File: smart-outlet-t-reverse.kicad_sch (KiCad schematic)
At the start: 4 parts

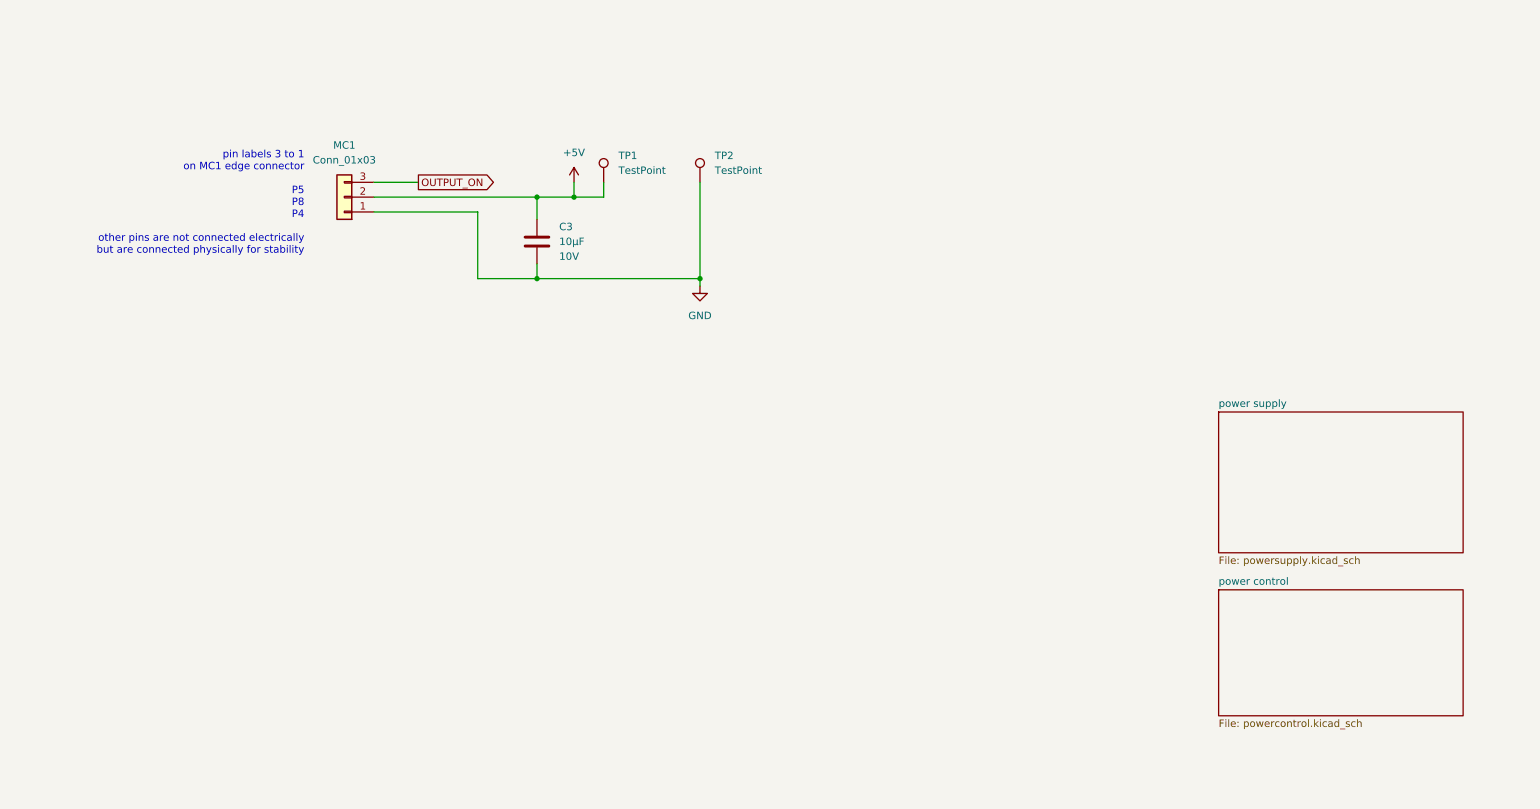
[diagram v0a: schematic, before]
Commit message: Cleaned schematic. Still have silk and fab to do. Also have not fixed F1. Have decided I may not fix F1.
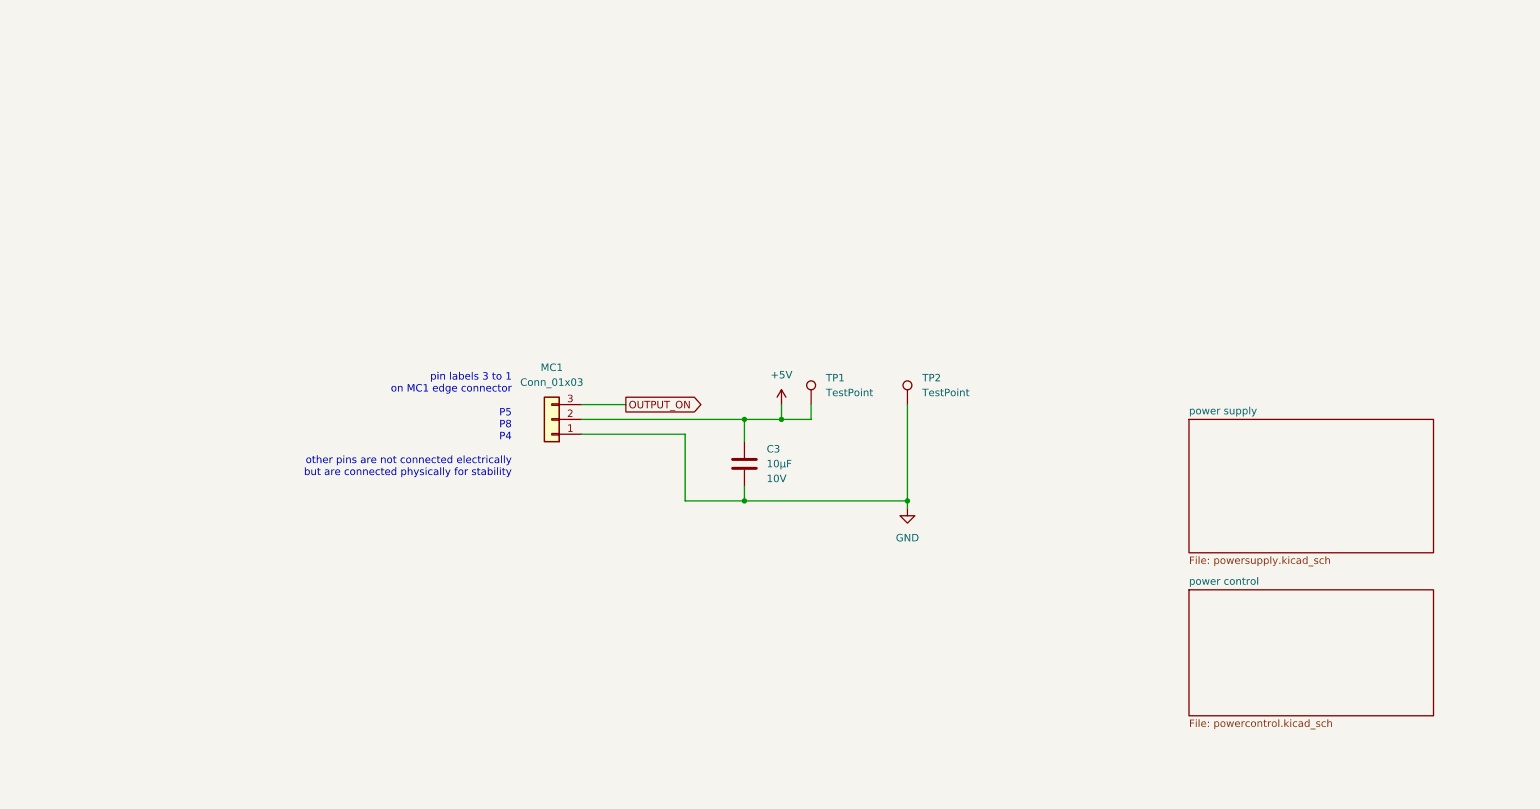
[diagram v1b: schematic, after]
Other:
- title: (none) -> T smart switched power outlet
- moved on the sheet: C3, MC1, TP1, TP2

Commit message: Added description of microcontroller subboard to schematic.
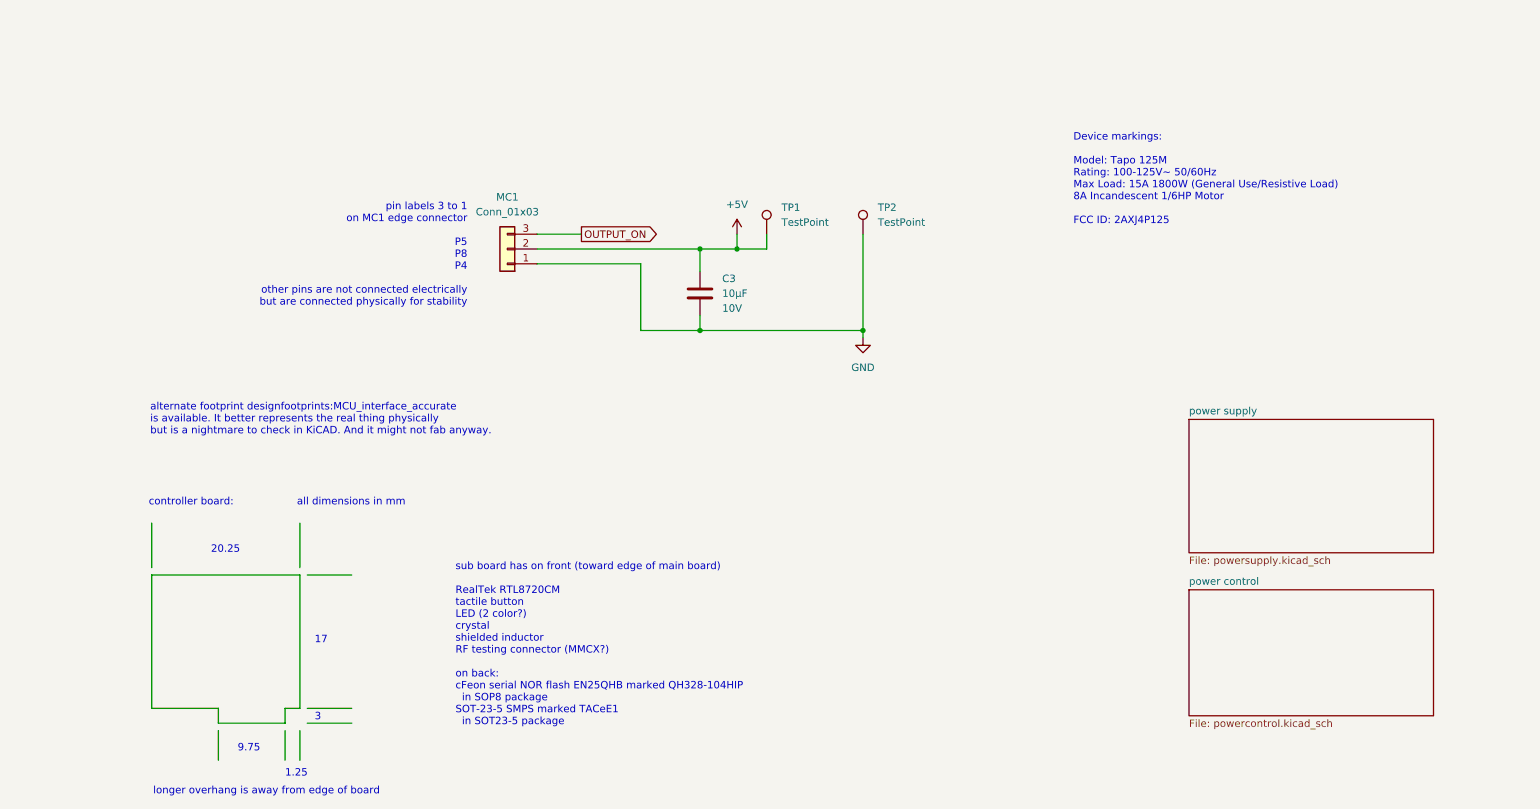
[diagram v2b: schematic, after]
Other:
- note added: "1.25"
- note added: "17"
- note added: "20.25"
- note added: "3"
- note added: "9.75"
- note added: "Device markings: Model: Tapo 125M Rating: 100-125V~ 50/60Hz Max Load: 15A 1800W (General Use/Resistive Load) 8A Incandescent 1/6HP Motor FCC ID: 2AXJ4P125"
- note added: "all dimensions in mm"
- note added: "alternate footprint designfootprints:MCU_interface_accurate is available. It better represents the real thing physically but is a nightmare to check in KiCAD. And it might not fab anyway."
- note added: "controller board:"
- note added: "longer overhang is away from edge of board"
- note added: "sub board has on front (toward edge of main board) RealTek RTL8720CM tactile button LED (2 color?) crystal shielded inductor RF testing connector (MMCX?) on back: cFeon serial NOR flash EN25QHB marked QH328-104HIP in SOP8 package SOT-23-5 SMPS marked TACeE1 in SOT23-5 package"
- moved on the sheet: C3, MC1, TP1, TP2

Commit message: Updating project to describe itself better.
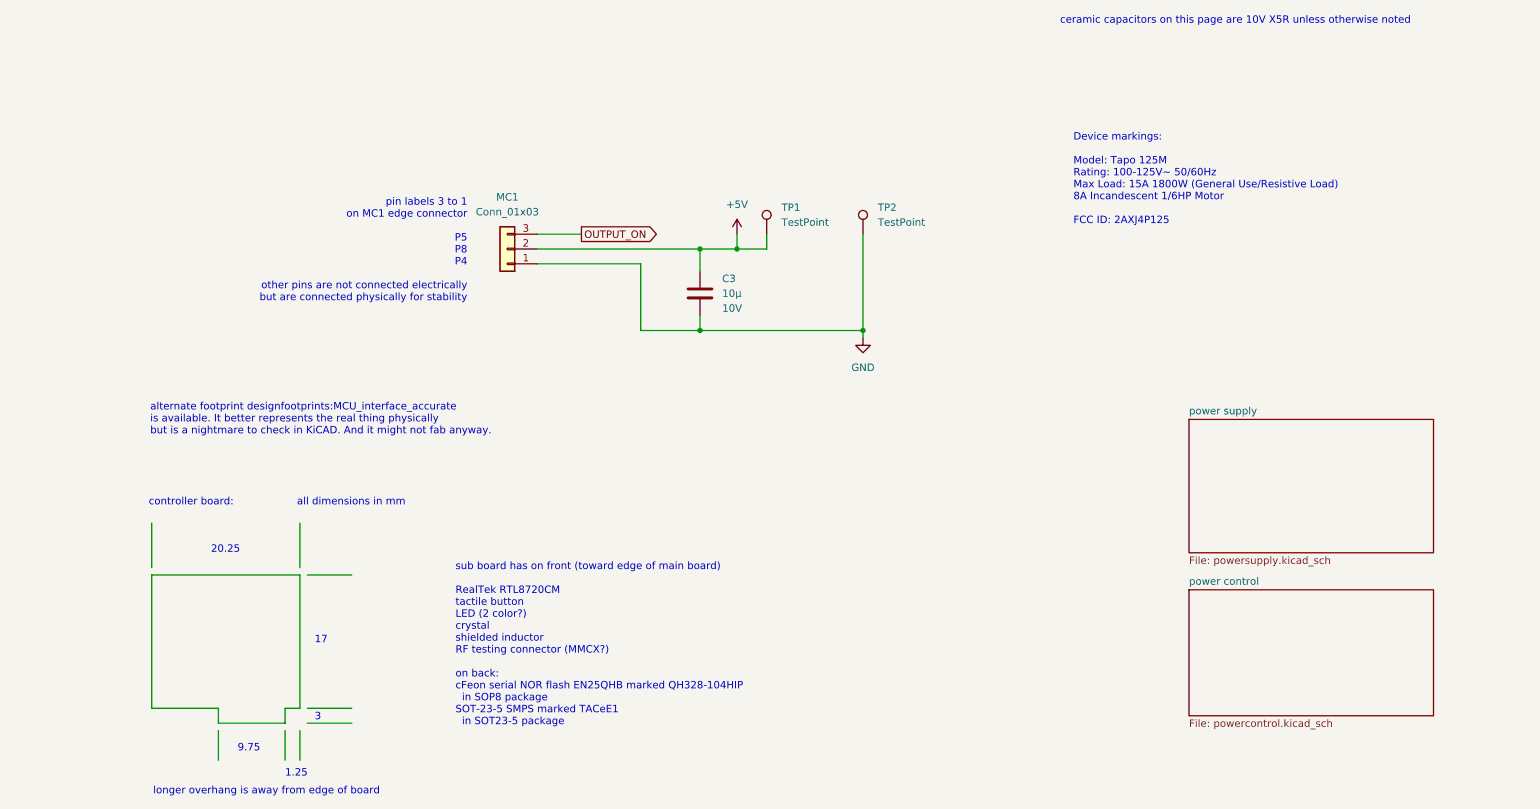
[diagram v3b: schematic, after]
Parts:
- C3: value 10µF -> 10µ
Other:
- note added: "ceramic capacitors on this page are 10V X5R unless otherwise noted"
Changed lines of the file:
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@@
 	(title_block
 		(title "T smart switched power outlet")
-		(date "2025-08-01")
+		(date "2025-08-17")
+		(rev "a")
 	)
 	(text "pin labels 3 to 1\non MC1 edge connector\n\nP5\nP8\nP4\n\nother pins are not connected electrically\nbut are connected physically for stability"
 		(exclude_from_sim no)
-		(at 92.202 59.436 0)
+		(at 92.202 58.674 0)
 		(effects
 			(font
@@
 		(exclude_from_sim no)
 		(at 48.26 109.982 0)
+		(effects
+			(font
+				(size 1.27 1.27)
+			)
+			(justify left)
+		)
+	)
+	(text "ceramic capacitors on this page are 10V X5R unless otherwise noted"
+		(exclude_from_sim no)
+		(at 193.802 19.304 0)
 		(effects
 			(font
@@
 			)
 		)
-		(property "Value" "10µF"
+		(property "Value" "10µ"
 			(at 135.89 66.0399 0)
 			(effects

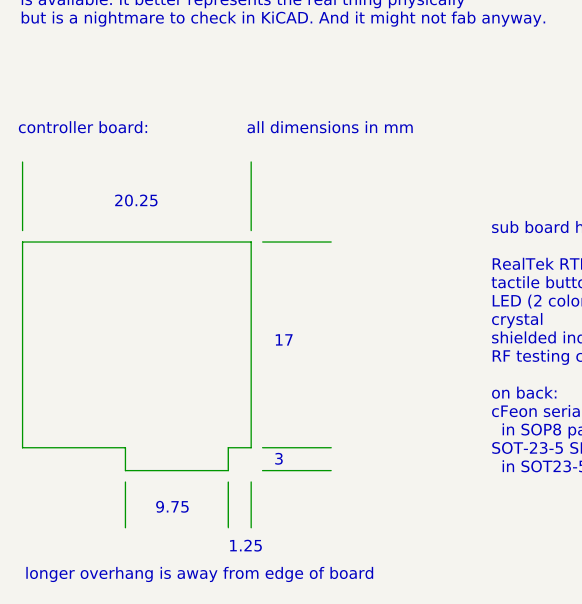
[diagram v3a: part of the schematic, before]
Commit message: Updated README to be more detailed. Updated schematic to pass checks and regenerated PDF. Added a few comments. Updated pcb from schematic changes.
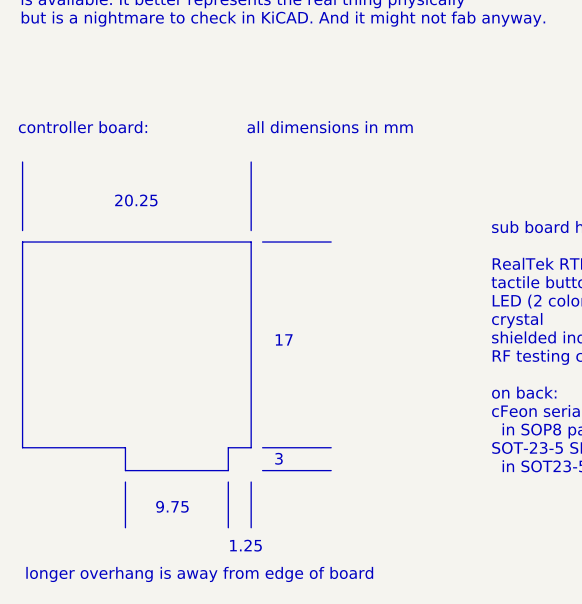
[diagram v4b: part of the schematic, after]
